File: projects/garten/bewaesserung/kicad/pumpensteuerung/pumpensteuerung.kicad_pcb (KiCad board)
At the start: 2 copper layers, 100 x 85 mm, 35 parts, among them J101 Screw_Terminal_01x02, J201 Screw_Terminal_01x03, J301 Screw_Terminal_01x03, J401 Screw_Terminal_01x03, J501 Screw_Terminal_01x03, K201 SANYOU_SRD_Form_C, K301 SANYOU_SRD_Form_C, K401 SANYOU_SRD_Form_C, K501 SANYOU_SRD_Form_C, Q201 2N3904, Q301 2N3904, Q401 2N3904, Q501 2N3904, U101 LM2575-5.0BT

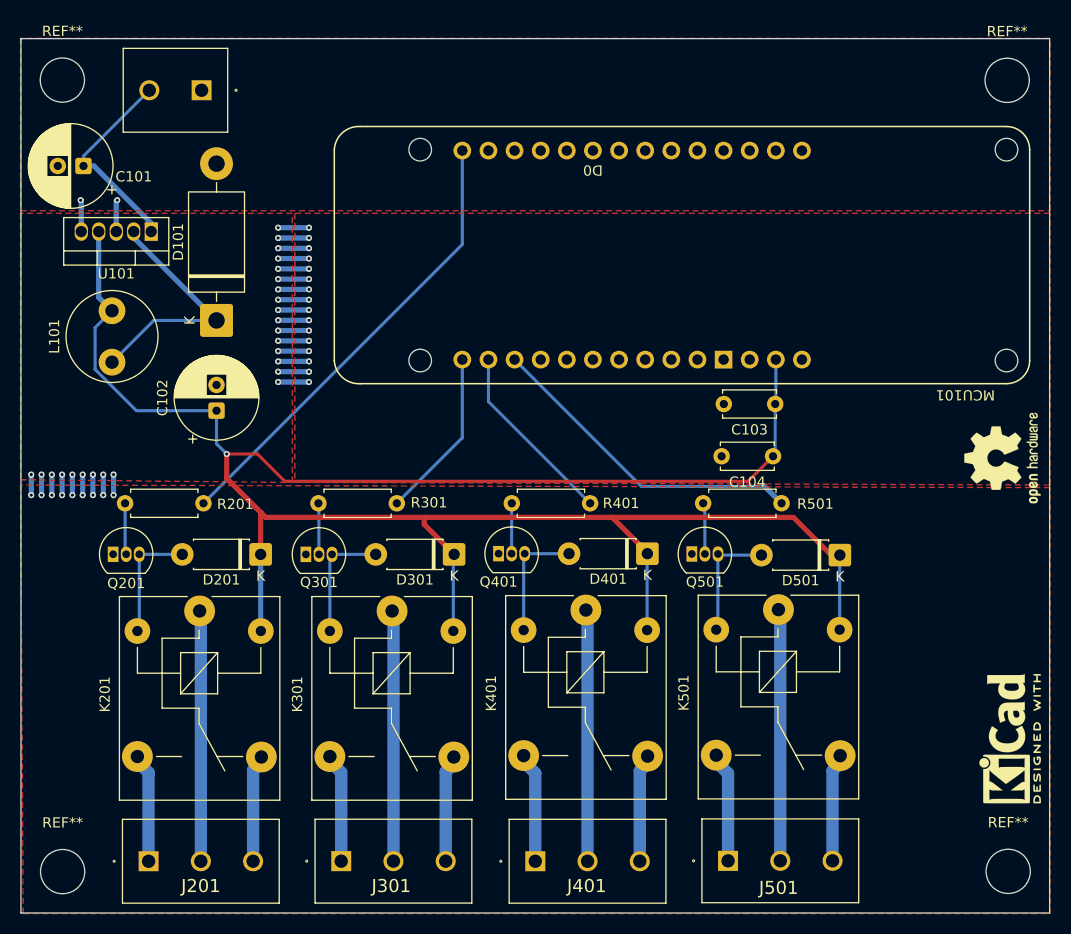
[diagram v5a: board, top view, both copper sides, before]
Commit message: [garten/bewaesserung(pcb)] remove capacitor and more space at the top
bloed wenn man nicht misst und gehaeuse und pcb unabhaenig desgin und so
dann erst wenn es fertig ist feststellt da passt etwas nicht. wobei der
arduino ja auch im 3d model des pcb fehlt :(.
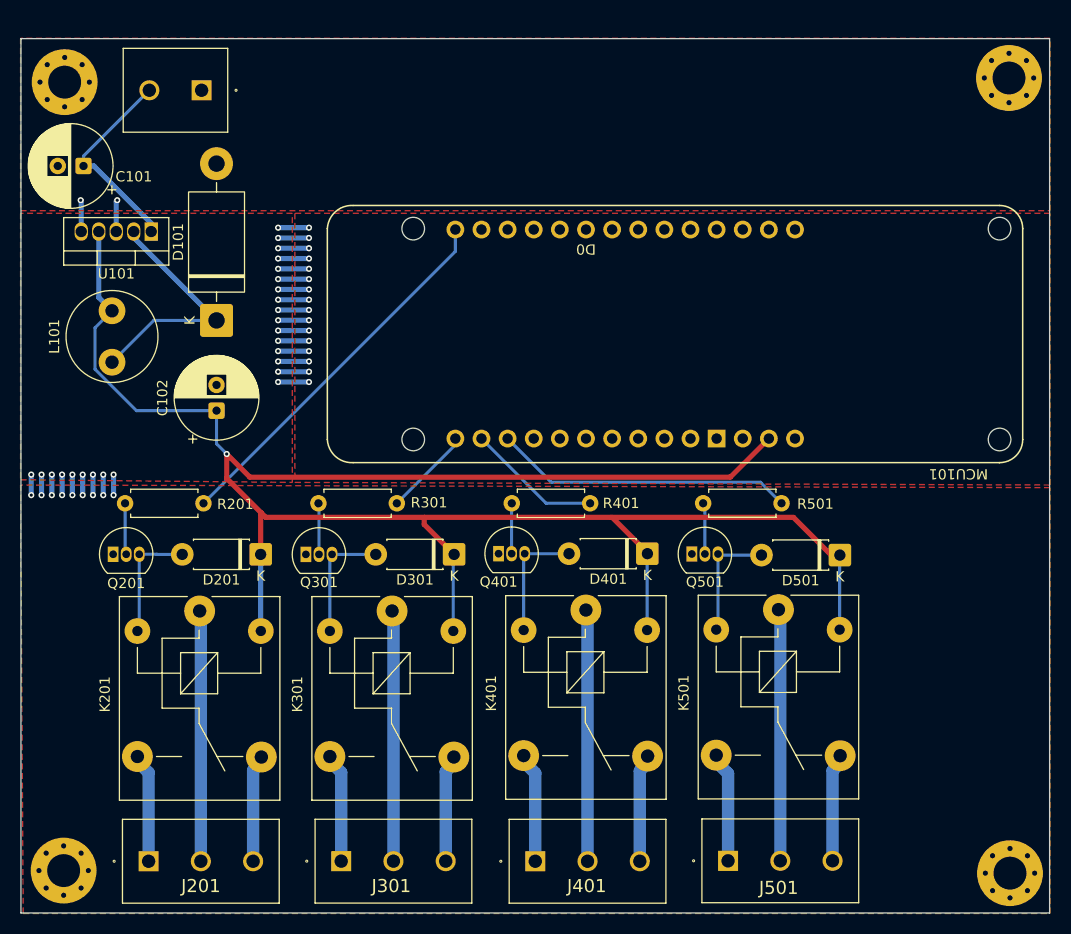
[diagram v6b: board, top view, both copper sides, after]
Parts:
- removed C103: 0.1uF 500V +80/-20%, Capacitor_THT:C_Disc_D5.0mm_W2.5mm_P5.00mm
- removed C104: 10000pF 100V 10% Y5P 5mm, Capacitor_THT:C_Disc_D5.0mm_W2.5mm_P5.00mm
- removed REF** (x4): MountingHole_4.3mm_M4_DIN965, MountingHole:MountingHole_4.3mm_M4_DIN965
- removed REF**: KiCad-Logo2_5mm_SilkScreen, Symbol:KiCad-Logo2_5mm_SilkScreen
- removed REF**: OSHW-Logo2_9.8x8mm_SilkScreen, Symbol:OSHW-Logo2_9.8x8mm_SilkScreen
- added H101: M3, MountingHole:MountingHole_3.2mm_M3_Pad_Via, F.Cu at (54.8, 53.2)
- added H102: M3, MountingHole:MountingHole_3.2mm_M3_Pad_Via, F.Cu at (54.6, 129.9)
- added H103: M3, MountingHole:MountingHole_3.2mm_M3_Pad_Via, F.Cu at (146.7, 130.1)
- added H104: M3, MountingHole:MountingHole_3.2mm_M3_Pad_Via, F.Cu at (146.6, 52.8)
- moved MCU101 7.71 mm to (145.6, 88.0)
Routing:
- net /+5V: track 206.9 -> 197.3 mm
- net /Bewaesserungsrelais: track 16.6 -> 8.65 mm
- net /Hauptrelais: track 44.7 -> 36.8 mm
- net /Poolrelais: track 18.1 -> 13.2 mm
- net /Poolvollrelais: track 31.7 -> 29.2 mm
